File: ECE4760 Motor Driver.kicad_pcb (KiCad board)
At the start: 6 copper layers, 43.2 x 44.5 mm, 162 parts, among them J1 IO, J101 Alternative Motor, J2 Motor / Power, J3 UART, Q1 EPC23104, Q2 EPC23104, Q3 EPC23104, Q4 EPC23104, U1 STM32G473V_B-C-E_Hx, U2 ACS711xEXLT-15AB, U3 ACS711xEXLT-15AB, U4 ACS711xEXLT-15AB, U5 ACS711xEXLT-15AB, U6 AP7361C-33FGE, U7 TPSM365R6, X1 48MHz

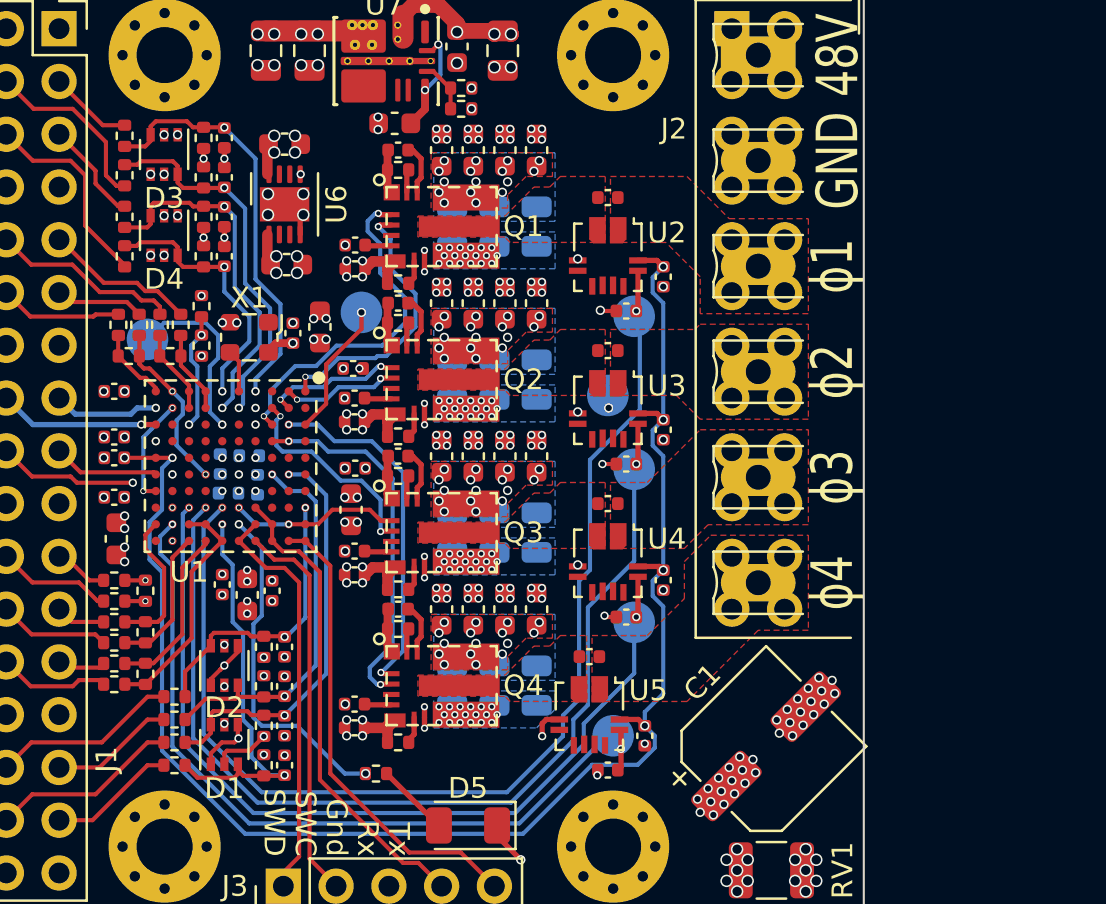
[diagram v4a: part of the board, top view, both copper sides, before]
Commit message: Change MCU package and MOSFETs
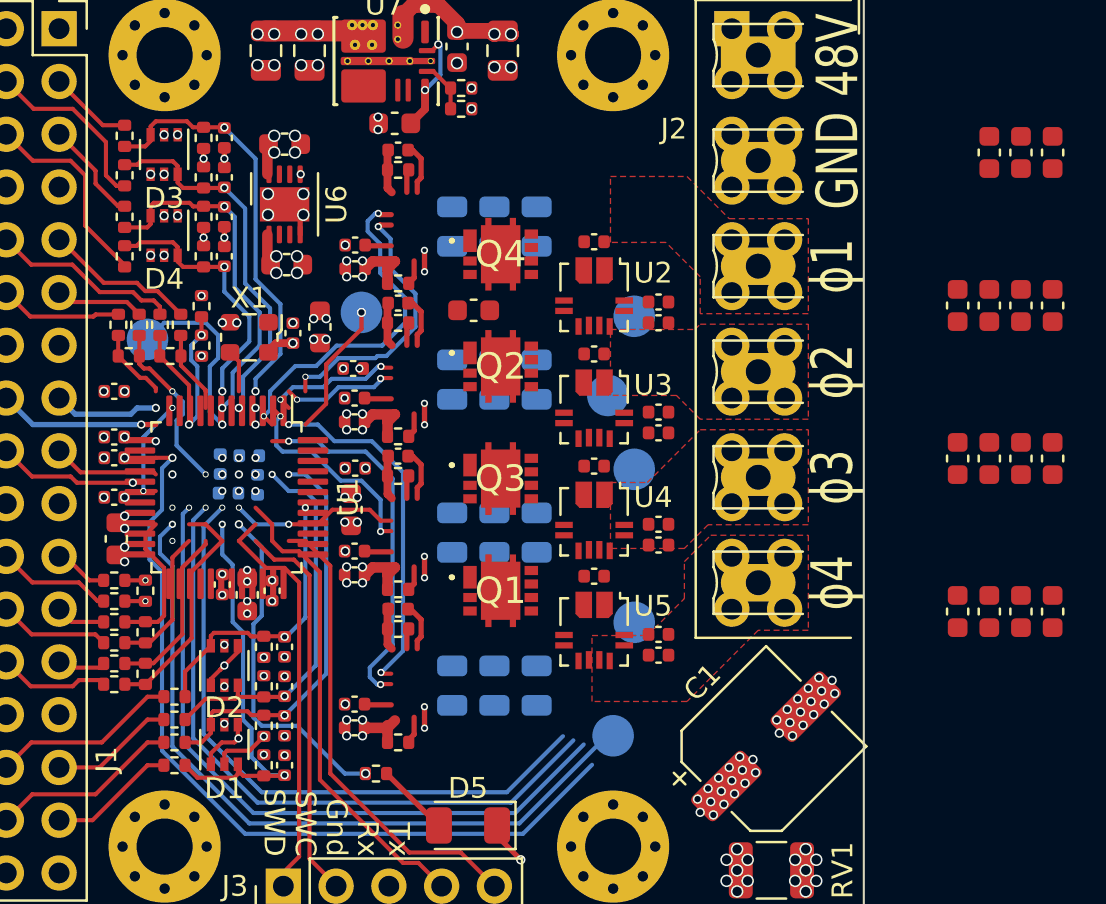
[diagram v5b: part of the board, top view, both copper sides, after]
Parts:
- Q1, Q2, Q3, Q4: value EPC23104 -> CSD87333Q3D; footprint EPC:EPC2310x -> CSD87333Q3D:CSD87333Q3D
- U1: value STM32G473V_B-C-E_Hx -> STM32G473CETx; footprint Package_BGA:TFBGA-100_8x8mm_Layout10x10_P0.8mm -> Package_QFP:LQFP-48_7x7mm_P0.5mm
- moved C12 24.8 mm to (128.5, 48.5)
- moved C22 24.8 mm to (123.9, 55.9)
- moved C23 24.8 mm to (125.4, 55.9)
- moved C25 24.8 mm to (128.5, 55.9)
- moved C35 24.8 mm to (123.9, 63.2)
- moved C36 24.8 mm to (125.4, 63.2)
- moved C38 24.8 mm to (128.5, 63.2)
- moved C48 24.8 mm to (123.9, 70.6)
- moved C49 24.8 mm to (125.4, 70.6)
- moved C51 24.8 mm to (128.5, 70.6)
- moved C9 24.8 mm to (125.4, 48.5)
- moved C11 24.8 mm to (126.9, 48.5)
- moved C24 24.8 mm to (126.9, 55.9)
- moved C37 24.8 mm to (126.9, 63.2)
- moved C50 24.8 mm to (126.9, 70.6)
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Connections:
- C17 pad 2: Net-(Q1-V_{DD}) -> unconnected-(C17-Pad2)
- C18 pad 1: Net-(Q1-V_{PHASE}) -> unconnected-(C18-Pad1)
- C18 pad 2: Net-(Q1-V_{BOOT}) -> Net-(C18-Pad2)
- C19 pad 1: Net-(Q1-SW) -> Net-(U2-IP-)
- C30 pad 2: Net-(Q2-V_{DD}) -> unconnected-(C30-Pad2)
- C31 pad 1: Net-(Q2-V_{PHASE}) -> unconnected-(C31-Pad1)
- C31 pad 2: Net-(Q2-V_{BOOT}) -> Net-(C31-Pad2)
- C32 pad 1: Net-(Q2-SW) -> Net-(U3-IP-)
- C43 pad 2: Net-(Q3-V_{DD}) -> unconnected-(C43-Pad2)
- C44 pad 1: Net-(Q3-V_{PHASE}) -> unconnected-(C44-Pad1)
- C44 pad 2: Net-(Q3-V_{BOOT}) -> Net-(C44-Pad2)
- C45 pad 1: Net-(Q3-SW) -> Net-(U4-IP-)
- C56 pad 2: Net-(Q4-V_{DD}) -> unconnected-(C56-Pad2)
- C57 pad 1: Net-(Q4-V_{PHASE}) -> unconnected-(C57-Pad1)
- C57 pad 2: Net-(Q4-V_{BOOT}) -> Net-(C57-Pad2)
- C58 pad 1: Net-(Q4-SW) -> Net-(U5-IP-)
- Q1 pad 1: /PH1_HI -> unconnected-(Q1-VIN-Pad1)
- Q1 pad 10: Vdrive -> unconnected-(Q1-PGND_2-Pad10)
- Q1 pad 11: Net-(Q1-V_{PHASE}) -> unconnected-(Q1-PGND_3-Pad11)
- Q1 pad 12: Net-(Q1-R_{BOOT}) -> unconnected-(Q1-PGND_4-Pad12)
- Q1 pad 13: Net-(Q1-V_{BOOT}) -> unconnected-(Q1-PGND_5-Pad13)
- Q1 pad 4: Net-(Q1-V_{DD}) -> unconnected-(Q1-TGR-Pad4)
- Q1 pad 5: +5V -> unconnected-(Q1-BG-Pad5)
- Q1 pad 6: Net-(Q1-R_{DRV}) -> unconnected-(Q1-VSW_1-Pad6)
- Q1 pad 7: GND -> unconnected-(Q1-VSW_2-Pad7)
- Q1 pad 8: GND -> unconnected-(Q1-VSW_3-Pad8)
- Q1 pad 9: Net-(Q1-SW) -> unconnected-(Q1-PGND_1-Pad9)
- Q2 pad 1: /PH2_HI -> unconnected-(Q2-VIN-Pad1)
- Q2 pad 10: Vdrive -> unconnected-(Q2-PGND_2-Pad10)
- Q2 pad 11: Net-(Q2-V_{PHASE}) -> unconnected-(Q2-PGND_3-Pad11)
- Q2 pad 12: Net-(Q2-R_{BOOT}) -> unconnected-(Q2-PGND_4-Pad12)
- Q2 pad 13: Net-(Q2-V_{BOOT}) -> unconnected-(Q2-PGND_5-Pad13)
- Q2 pad 4: Net-(Q2-V_{DD}) -> unconnected-(Q2-TGR-Pad4)
- Q2 pad 5: +5V -> unconnected-(Q2-BG-Pad5)
- Q2 pad 6: Net-(Q2-R_{DRV}) -> unconnected-(Q2-VSW_1-Pad6)
- Q2 pad 7: GND -> unconnected-(Q2-VSW_2-Pad7)
- Q2 pad 8: GND -> unconnected-(Q2-VSW_3-Pad8)
- Q2 pad 9: Net-(Q2-SW) -> unconnected-(Q2-PGND_1-Pad9)
- Q3 pad 1: /PH3_HI -> unconnected-(Q3-VIN-Pad1)
- Q3 pad 10: Vdrive -> unconnected-(Q3-PGND_2-Pad10)
- Q3 pad 11: Net-(Q3-V_{PHASE}) -> unconnected-(Q3-PGND_3-Pad11)
- Q3 pad 12: Net-(Q3-R_{BOOT}) -> unconnected-(Q3-PGND_4-Pad12)
- Q3 pad 13: Net-(Q3-V_{BOOT}) -> unconnected-(Q3-PGND_5-Pad13)
- Q3 pad 4: Net-(Q3-V_{DD}) -> unconnected-(Q3-TGR-Pad4)
- Q3 pad 5: +5V -> unconnected-(Q3-BG-Pad5)
- Q3 pad 6: Net-(Q3-R_{DRV}) -> unconnected-(Q3-VSW_1-Pad6)
- Q3 pad 7: GND -> unconnected-(Q3-VSW_2-Pad7)
- Q3 pad 8: GND -> unconnected-(Q3-VSW_3-Pad8)
- Q3 pad 9: Net-(Q3-SW) -> unconnected-(Q3-PGND_1-Pad9)
- Q4 pad 1: /PH4_HI -> unconnected-(Q4-VIN-Pad1)
- Q4 pad 10: Vdrive -> unconnected-(Q4-PGND_2-Pad10)
- Q4 pad 11: Net-(Q4-V_{PHASE}) -> unconnected-(Q4-PGND_3-Pad11)
- Q4 pad 12: Net-(Q4-R_{BOOT}) -> unconnected-(Q4-PGND_4-Pad12)
- Q4 pad 13: Net-(Q4-V_{BOOT}) -> unconnected-(Q4-PGND_5-Pad13)
- Q4 pad 4: Net-(Q4-V_{DD}) -> unconnected-(Q4-TGR-Pad4)
- Q4 pad 5: +5V -> unconnected-(Q4-BG-Pad5)
- Q4 pad 6: Net-(Q4-R_{DRV}) -> unconnected-(Q4-VSW_1-Pad6)
- Q4 pad 7: GND -> unconnected-(Q4-VSW_2-Pad7)
- Q4 pad 8: GND -> unconnected-(Q4-VSW_3-Pad8)
- Q4 pad 9: Net-(Q4-SW) -> unconnected-(Q4-PGND_1-Pad9)
- R10 pad 2: Net-(Q4-R_{DRV}) -> unconnected-(R10-Pad2)
- R11 pad 1: Net-(Q4-R_{BOOT}) -> unconnected-(R11-Pad1)
- R11 pad 2: Net-(Q4-V_{BOOT}) -> Net-(C57-Pad2)
- R30 pad 2: Net-(U1-PC9) -> unconnected-(R30-Pad2)
- R4 pad 2: Net-(Q1-R_{DRV}) -> unconnected-(R4-Pad2)
- R5 pad 1: Net-(Q1-R_{BOOT}) -> unconnected-(R5-Pad1)
- R5 pad 2: Net-(Q1-V_{BOOT}) -> Net-(C18-Pad2)
- R6 pad 2: Net-(Q2-R_{DRV}) -> unconnected-(R6-Pad2)
- R7 pad 1: Net-(Q2-R_{BOOT}) -> unconnected-(R7-Pad1)
- R7 pad 2: Net-(Q2-V_{BOOT}) -> Net-(C31-Pad2)
- R8 pad 2: Net-(Q3-R_{DRV}) -> unconnected-(R8-Pad2)
- R9 pad 1: Net-(Q3-R_{BOOT}) -> unconnected-(R9-Pad1)
- R9 pad 2: Net-(Q3-V_{BOOT}) -> Net-(C44-Pad2)
- U2 pad 2: Net-(Q1-SW) -> Net-(U2-IP-)
- U3 pad 2: Net-(Q2-SW) -> Net-(U3-IP-)
- U4 pad 2: Net-(Q3-SW) -> Net-(U4-IP-)
- U5 pad 2: Net-(Q4-SW) -> Net-(U5-IP-)
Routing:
- net (no net): track 0.00 -> 95.3 mm, vias 0 -> 16
- net +3V3: track 83.9 -> 50.2 mm, vias 30 -> 25
- net /PH1_SENSE: track 54.7 -> 30.9 mm, vias 2 -> 1
- net /PH4_LO: track 17.8 -> 0.00 mm, vias 2 -> 0
- net /PH4_HI: track 17.1 -> 0.00 mm, vias 2 -> 0
- net /PH1_HI: track 16.7 -> 0.00 mm, vias 2 -> 0
- net unconnected-(R30-Pad2): track 0.00 -> 16.4 mm, vias 0 -> 2
- net Net-(U1-PC9): track 16.4 -> 0.00 mm, vias 2 -> 0
- net /PH2_SENSE: track 48.4 -> 32.2 mm, vias 2 -> 1
- net /PH1_LO: track 13.2 -> 0.00 mm, vias 2 -> 0
- net /PH3_LO: track 10.2 -> 0.00 mm, vias 2 -> 0
- net /PH3_SENSE: track 42.4 -> 33.5 mm, vias 2 -> 1
- net /PH3_HI: track 8.17 -> 0.00 mm, vias 2 -> 0
- net /PH2_HI: track 6.59 -> 0.00 mm, vias 2 -> 0
- net /PH2_LO: track 5.59 -> 0.00 mm, vias 2 -> 0
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- removed copper zone on B.Cu, net GND
- removed copper zone on F.Cu, net Net-(Q1-SW)
- removed copper zone on F.Cu, net Net-(Q2-SW)
- removed copper zone on F.Cu, net Net-(Q3-SW)
- removed copper zone on F.Cu, net Net-(Q4-SW)
- removed copper zone on B.Cu, net Vdrive
- removed copper zone on F.Cu, net Vdrive

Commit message: Update
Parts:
- removed C14, C15, C26, C27, C28, C3, C39, C40, C41, C52, C53, C54: 1u, 100V, 0805, X7R, Capacitor_SMD:C_0805_2012Metric
- removed C17, C30, C43, C56, C68, C69, C74, C75, C76, C77, C78, C79, C80, C81, C82, C83, C84: 100n, Capacitor_SMD:C_0402_1005Metric
- removed C2, C23, C24, C25, C36, C37, C38, C49, C50, C51: 100n, 100V, 0603, X7R, Capacitor_SMD:C_0603_1608Metric
- removed C4, C5: 22u, Capacitor_SMD:C_0805_2012Metric
- removed C64: 1n, Capacitor_SMD:C_0402_1005Metric
- removed C7, C70, C71, C72, C73: 4u7, Capacitor_SMD:C_0603_1608Metric
- removed D1, D2, D3, D4: BAT54XY, Package_TO_SOT_SMD:SOT-363_SC-70-6
- removed R1: 40k2, Resistor_SMD:R_0402_1005Metric
- removed R18, R26: 4k7, Resistor_SMD:R_0402_1005Metric
- removed R19, R27: 100, Resistor_SMD:R_0402_1005Metric
- removed R28, R29: 1k, Resistor_SMD:R_0402_1005Metric
- removed R3: 10k, Resistor_SMD:R_0402_1005Metric
- removed R40, R41, R42, R43, R44, R45: 1k, 1%, Resistor_SMD:R_0402_1005Metric
- removed TP1: RESET, TestPoint:TestPoint_Pad_D2.0mm
- removed TP2: BOOT, TestPoint:TestPoint_Pad_D2.0mm
- removed U7: TPSM365R6, TPSM:RDN0011A-MFG
- added D6: Green, LED_SMD:LED_1206_3216Metric, F.Cu at (112.1, 43.3)
- added L1: 4u7, Inductor_SMD:L_1008_2520Metric, F.Cu at (89.4, 70.8)
- added R2: 330, Resistor_SMD:R_0402_1005Metric, F.Cu at (95.4, 81.4)
- added SW1: RESET, Button_Switch_SMD:SW_SPST_PTS810, F.Cu at (100.8, 43.2)
- added U10: DGD05473FNQ, Package_DFN_QFN:DFN-10-1EP_3x3mm_P0.5mm_EP1.65x2.38mm, F.Cu at (94.1, 55.0)
- added U11: DGD05473FNQ, Package_DFN_QFN:DFN-10-1EP_3x3mm_P0.5mm_EP1.65x2.38mm, F.Cu at (94.1, 60.4)
- added U12: DGD05473FNQ, Package_DFN_QFN:DFN-10-1EP_3x3mm_P0.5mm_EP1.65x2.38mm, F.Cu at (94.1, 65.8)
- added U13: AP63205WU, Package_TO_SOT_SMD:TSOT-23-6, F.Cu at (89.4, 74.8)
- added U8: DGD05473FNQ, Package_DFN_QFN:DFN-10-1EP_3x3mm_P0.5mm_EP1.65x2.38mm, F.Cu at (94.1, 49.6)
- added U9: MAX13433EETD, Package_DFN_QFN:DFN-14-1EP_3x3mm_P0.4mm_EP1.78x2.35mm, F.Cu at (82.8, 69.2)
- C1: footprint Capacitor_SMD:CP_Elec_6.3x7.7 -> Capacitor_THT:CP_Radial_D6.3mm_P2.50mm
- C10, C11: value 100n, 100V, 0603, X7R -> 22u; footprint Capacitor_SMD:C_0603_1608Metric -> Capacitor_SMD:C_0805_2012Metric
- C12: value 100n, 100V, 0603, X7R -> 10u; footprint Capacitor_SMD:C_0603_1608Metric -> Capacitor_SMD:C_0805_2012Metric
- C13: value 1u, 100V, 0805, X7R -> 100n; footprint Capacitor_SMD:C_0805_2012Metric -> Capacitor_SMD:C_0402_1005Metric; moved to F.Cu
- C16, C29, C42, C55: value 1u -> 100n
- J1: footprint Connector_PinSocket_2.54mm:PinSocket_2x17_P2.54mm_Vertical -> Connector_PinSocket_2.54mm:PinSocket_2x14_P2.54mm_Vertical
- J3: footprint Connector_PinHeader_2.54mm:PinHeader_1x05_P2.54mm_Vertical -> Connector_PinHeader_2.54mm:PinHeader_2x04_P2.54mm_Vertical
- RV1: value 60V 250A -> 26V 200A
- moved C11 45.7 mm to (87.0, 70.6), turned to -90 degrees
- moved C12 44.9 mm to (92.1, 74.8)
- moved D5 41.4 mm to (117.6, 43.3), turned to -90 degrees
- moved J3 38.9 mm to (87.9, 45.1)
- moved R15 30.4 mm to (80.8, 48.1), turned to -90 degrees
- moved J101 29.7 mm to (141.2, 51.9)
- moved R14 29.6 mm to (80.8, 50.0), turned to 90 degrees
- moved R13 29.1 mm to (81.8, 48.1), turned to -90 degrees
- moved C62 28.2 mm to (80.8, 51.9), turned to -90 degrees
- moved R12 27.5 mm to (81.8, 50.0)
- moved R17 26.8 mm to (82.8, 48.1), turned to -90 degrees
- moved C61 26.1 mm to (81.8, 51.9)
- moved C9 24.7 mm to (100.8, 46.7), turned to 0 degrees
- moved C13 24.6 mm to (87.2, 73.3), turned to 90 degrees
- moved C48 24.3 mm to (100.8, 62.9), turned to 0 degrees
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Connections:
- net LED_1 renamed CLK+
- net LED_2 renamed CLK-
- net ~{Abort} renamed DATA-
- C10 pad 1: Vdrive -> +5V
- C11 pad 1: Vdrive -> +5V
- C13 pad 1: Vdrive -> Net-(U13-BST)
- C13 pad 2: GND -> Net-(U13-SW)
- C18 pad 1: unconnected-(C18-Pad1) -> Net-(U8-VB)
- C18 pad 2: Net-(C18-Pad2) -> Net-(Q1-TGR)
- C31 pad 1: unconnected-(C31-Pad1) -> Net-(U10-VB)
- C31 pad 2: Net-(C31-Pad2) -> Net-(Q2-TGR)
- C44 pad 1: unconnected-(C44-Pad1) -> Net-(U11-VB)
- C44 pad 2: Net-(C44-Pad2) -> Net-(Q3-TGR)
- C57 pad 1: unconnected-(C57-Pad1) -> Net-(U12-VB)
- C57 pad 2: Net-(C57-Pad2) -> Net-(Q4-TGR)
- C61 pad 1: /HALL_C -> /HALL_B
- C62 pad 1: /HALL_I -> /HALL_C
- C63 pad 1: /HALL_B -> /HALL_A
- J1 pad 1: +5V -> unconnected-(J1-Pin_1-Pad1)
- J1 pad 10: Aux_Enc_B_In- -> Hall_B_In
- J1 pad 11: Aux_Enc_A_In- -> Hall_I_In
- J1 pad 12: Aux_Enc_A_In+ -> Hall_C_In
- J1 pad 13: +5V -> unconnected-(J1-Pin_13-Pad13)
- J1 pad 14: GND -> unconnected-(J1-Pin_14-Pad14)
- J1 pad 17: ~{Fault_Enable} -> DATA+
- J1 pad 19: +3V3 -> unconnected-(J1-Pin_19-Pad19)
- J1 pad 2: GND -> unconnected-(J1-Pin_2-Pad2)
- J1 pad 20: GND -> unconnected-(J1-Pin_20-Pad20)
- J1 pad 27: +5V -> unconnected-(J1-Pin_27-Pad27)
- J1 pad 28: GND -> unconnected-(J1-Pin_28-Pad28)
- J1 pad 7: +5V -> unconnected-(J1-Pin_7-Pad7)
- J1 pad 8: GND -> unconnected-(J1-Pin_8-Pad8)
- J1 pad 9: Aux_Enc_B_In+ -> Hall_A_In
- J2 pad 1: Vdrive -> PH1
- J2 pad 2: GND -> PH2
- J2 pad 3: PH1 -> PH3
- J2 pad 4: PH2 -> PH4
- J2 pad 5: PH3 -> Vdrive
- J2 pad 6: PH4 -> GND
- J3 pad 2: /UART_TX -> /SWCLK
- J3 pad 3: GND -> /UART_TX
- J3 pad 5: /SWCLK -> GND
- Q1 pad 1: unconnected-(Q1-VIN-Pad1) -> Vdrive
- Q1 pad 10: unconnected-(Q1-PGND_2-Pad10) -> GND
- Q1 pad 11: unconnected-(Q1-PGND_3-Pad11) -> GND
- Q1 pad 12: unconnected-(Q1-PGND_4-Pad12) -> GND
- Q1 pad 13: unconnected-(Q1-PGND_5-Pad13) -> GND
- Q1 pad 3: unconnected-(Q1-TG-Pad3) -> Net-(Q1-TG)
- Q1 pad 4: unconnected-(Q1-TGR-Pad4) -> Net-(Q1-TGR)
- Q1 pad 5: unconnected-(Q1-BG-Pad5) -> Net-(Q1-BG)
- Q1 pad 6: unconnected-(Q1-VSW_1-Pad6) -> Net-(U2-IP-)
- Q1 pad 7: unconnected-(Q1-VSW_2-Pad7) -> Net-(U2-IP-)
- Q1 pad 8: unconnected-(Q1-VSW_3-Pad8) -> Net-(U2-IP-)
- Q1 pad 9: unconnected-(Q1-PGND_1-Pad9) -> GND
- Q2 pad 1: unconnected-(Q2-VIN-Pad1) -> Vdrive
- Q2 pad 10: unconnected-(Q2-PGND_2-Pad10) -> GND
- Q2 pad 11: unconnected-(Q2-PGND_3-Pad11) -> GND
- Q2 pad 12: unconnected-(Q2-PGND_4-Pad12) -> GND
- Q2 pad 13: unconnected-(Q2-PGND_5-Pad13) -> GND
- Q2 pad 3: unconnected-(Q2-TG-Pad3) -> Net-(Q2-TG)
- Q2 pad 4: unconnected-(Q2-TGR-Pad4) -> Net-(Q2-TGR)
- Q2 pad 5: unconnected-(Q2-BG-Pad5) -> Net-(Q2-BG)
- Q2 pad 6: unconnected-(Q2-VSW_1-Pad6) -> Net-(U3-IP-)
- Q2 pad 7: unconnected-(Q2-VSW_2-Pad7) -> Net-(U3-IP-)
- Q2 pad 8: unconnected-(Q2-VSW_3-Pad8) -> Net-(U3-IP-)
- Q2 pad 9: unconnected-(Q2-PGND_1-Pad9) -> GND
- Q3 pad 1: unconnected-(Q3-VIN-Pad1) -> Vdrive
- Q3 pad 10: unconnected-(Q3-PGND_2-Pad10) -> GND
- Q3 pad 11: unconnected-(Q3-PGND_3-Pad11) -> GND
- Q3 pad 12: unconnected-(Q3-PGND_4-Pad12) -> GND
- Q3 pad 13: unconnected-(Q3-PGND_5-Pad13) -> GND
- Q3 pad 3: unconnected-(Q3-TG-Pad3) -> Net-(Q3-TG)
- Q3 pad 4: unconnected-(Q3-TGR-Pad4) -> Net-(Q3-TGR)
- Q3 pad 5: unconnected-(Q3-BG-Pad5) -> Net-(Q3-BG)
- Q3 pad 6: unconnected-(Q3-VSW_1-Pad6) -> Net-(U4-IP-)
- Q3 pad 7: unconnected-(Q3-VSW_2-Pad7) -> Net-(U4-IP-)
- Q3 pad 8: unconnected-(Q3-VSW_3-Pad8) -> Net-(U4-IP-)
- Q3 pad 9: unconnected-(Q3-PGND_1-Pad9) -> GND
- Q4 pad 1: unconnected-(Q4-VIN-Pad1) -> Vdrive
- Q4 pad 10: unconnected-(Q4-PGND_2-Pad10) -> GND
- Q4 pad 11: unconnected-(Q4-PGND_3-Pad11) -> GND
- Q4 pad 12: unconnected-(Q4-PGND_4-Pad12) -> GND
- Q4 pad 13: unconnected-(Q4-PGND_5-Pad13) -> GND
- Q4 pad 3: unconnected-(Q4-TG-Pad3) -> Net-(Q4-TG)
- Q4 pad 4: unconnected-(Q4-TGR-Pad4) -> Net-(Q4-TGR)
- Q4 pad 5: unconnected-(Q4-BG-Pad5) -> Net-(Q4-BG)
- Q4 pad 6: unconnected-(Q4-VSW_1-Pad6) -> Net-(U5-IP-)
- Q4 pad 7: unconnected-(Q4-VSW_2-Pad7) -> Net-(U5-IP-)
- Q4 pad 8: unconnected-(Q4-VSW_3-Pad8) -> Net-(U5-IP-)
- Q4 pad 9: unconnected-(Q4-PGND_1-Pad9) -> GND
- R10 pad 1: +5V -> Net-(Q4-TG)
- R10 pad 2: unconnected-(R10-Pad2) -> Net-(U12-HO)
- R11 pad 1: unconnected-(R11-Pad1) -> Net-(U12-LO)
- R11 pad 2: Net-(C57-Pad2) -> Net-(Q4-BG)
- R12 pad 2: /HALL_C -> /HALL_B
- R13 pad 1: Hall_C_In -> Hall_B_In
- R13 pad 2: /HALL_C -> /HALL_B
- R14 pad 2: /HALL_I -> /HALL_C
- R15 pad 1: Hall_I_In -> Hall_C_In
- R15 pad 2: /HALL_I -> /HALL_C
- R16 pad 2: /HALL_B -> /HALL_A
- R17 pad 1: Hall_B_In -> Hall_A_In
- R17 pad 2: /HALL_B -> /HALL_A
- R30 pad 1: Net-(D5-A) -> Net-(U1-PA6)
- R30 pad 2: unconnected-(R30-Pad2) -> Net-(D5-A)
- R31 pad 1: Enc_A_In+ -> Enc_I_In+
- R31 pad 2: /ENC_A+ -> /ENC_I+
- R32 pad 1: /ENC_A- -> /ENC_I-
- R32 pad 2: /ENC_A+ -> /ENC_I+
- R33 pad 1: Enc_A_In- -> Enc_I_In-
- R33 pad 2: /ENC_A- -> /ENC_I-
- R34 pad 1: Enc_B_In+ -> Enc_A_In+
- R34 pad 2: /ENC_B+ -> /ENC_A+
- R35 pad 1: /ENC_B- -> /ENC_A-
- R35 pad 2: /ENC_B+ -> /ENC_A+
- R36 pad 1: Enc_B_In- -> Enc_A_In-
- R36 pad 2: /ENC_B- -> /ENC_A-
- R37 pad 1: Enc_I_In+ -> Enc_B_In+
- R37 pad 2: /ENC_I+ -> /ENC_B+
- R38 pad 1: /ENC_I- -> /ENC_B-
- R38 pad 2: /ENC_I+ -> /ENC_B+
- R39 pad 1: Enc_I_In- -> Enc_B_In-
- R39 pad 2: /ENC_I- -> /ENC_B-
- R4 pad 1: +5V -> Net-(Q1-TG)
- R4 pad 2: unconnected-(R4-Pad2) -> Net-(U8-HO)
- R5 pad 1: unconnected-(R5-Pad1) -> Net-(U8-LO)
- R5 pad 2: Net-(C18-Pad2) -> Net-(Q1-BG)
- R6 pad 1: +5V -> Net-(Q2-TG)
- R6 pad 2: unconnected-(R6-Pad2) -> Net-(U10-HO)
- R7 pad 1: unconnected-(R7-Pad1) -> Net-(U10-LO)
- R7 pad 2: Net-(C31-Pad2) -> Net-(Q2-BG)
- R8 pad 1: +5V -> Net-(Q3-TG)
- R8 pad 2: unconnected-(R8-Pad2) -> Net-(U11-HO)
- R9 pad 1: unconnected-(R9-Pad1) -> Net-(U11-LO)
- R9 pad 2: Net-(C44-Pad2) -> Net-(Q3-BG)
- U1 pad 1: unconnected-(U1-VBAT-Pad1) -> +3V3
- U1 pad 10: unconnected-(U1-PA2-Pad10) -> /HALL_C
- U1 pad 11: unconnected-(U1-PA3-Pad11) -> Net-(U1-PA3)
- U1 pad 12: unconnected-(U1-PA4-Pad12) -> /ENC_I-
- U1 pad 13: unconnected-(U1-PA5-Pad13) -> /ENC_A-
- U1 pad 14: unconnected-(U1-PA6-Pad14) -> Net-(U1-PA6)
- U1 pad 15: unconnected-(U1-PA7-Pad15) -> /ENC_A+
- U1 pad 16: unconnected-(U1-PB0-Pad16) -> /ENC_B+
- U1 pad 17: unconnected-(U1-PB1-Pad17) -> /ENC_I+
- U1 pad 18: unconnected-(U1-PB2-Pad18) -> /ENC_B-
- U1 pad 19: unconnected-(U1-VSSA-Pad19) -> GND
- U1 pad 2: unconnected-(U1-PC13-Pad2) -> /LIM_L
- U1 pad 21: unconnected-(U1-VDDA-Pad21) -> +3V3
- U1 pad 23: Net-(U1-VSS-Pad23) -> GND
- U1 pad 24: unconnected-(U1-VDD-Pad24) -> +3V3
- U1 pad 25: unconnected-(U1-PB11-Pad25) -> /PH4_SENSE
- U1 pad 26: unconnected-(U1-PB12-Pad26) -> /PH3_SENSE
- U1 pad 27: unconnected-(U1-PB13-Pad27) -> /PH2_SENSE
- U1 pad 28: unconnected-(U1-PB14-Pad28) -> /PH1_SENSE
- U1 pad 29: unconnected-(U1-PB15-Pad29) -> /PH2_LO
- U1 pad 3: unconnected-(U1-PC14-Pad3) -> /LIM_R
- U1 pad 30: unconnected-(U1-PA8-Pad30) -> /PH4_HI
- U1 pad 31: unconnected-(U1-PA9-Pad31) -> /PH3_HI
- U1 pad 32: unconnected-(U1-PA10-Pad32) -> /PH2_HI
- U1 pad 33: unconnected-(U1-PA11-Pad33) -> /PH4_LO
- U1 pad 34: unconnected-(U1-PA12-Pad34) -> /PH3_LO
- U1 pad 35: Net-(U1-VSS-Pad23) -> GND
- U1 pad 36: unconnected-(U1-VDD-Pad36) -> +3V3
- U1 pad 37: unconnected-(U1-PA13-Pad37) -> /SWDIO
- U1 pad 38: unconnected-(U1-PA14-Pad38) -> /SWCLK
- U1 pad 39: unconnected-(U1-PA15-Pad39) -> ~{Fault_Enable}
- U1 pad 4: unconnected-(U1-PC15-Pad4) -> /LIM_H
- U1 pad 40: unconnected-(U1-PB3-Pad40) -> Net-(U1-PB3)
- U1 pad 41: unconnected-(U1-PB4-Pad41) -> Net-(U1-PB4)
- U1 pad 42: unconnected-(U1-PB5-Pad42) -> /PH1_LO
- U1 pad 43: unconnected-(U1-PB6-Pad43) -> /UART_TX
- U1 pad 44: unconnected-(U1-PB7-Pad44) -> /UART_RX
- U1 pad 45: unconnected-(U1-PB8-Pad45) -> /BOOT
- U1 pad 46: unconnected-(U1-PB9-Pad46) -> /PH1_HI
- U1 pad 47: Net-(U1-VSS-Pad23) -> GND
- U1 pad 48: unconnected-(U1-VDD-Pad48) -> +3V3
- U1 pad 5: unconnected-(U1-PF0-Pad5) -> /OSC_IN
- U1 pad 7: unconnected-(U1-PG10-Pad7) -> /~{RST}
- U1 pad 8: unconnected-(U1-PA0-Pad8) -> /HALL_A
- U1 pad 9: unconnected-(U1-PA1-Pad9) -> /HALL_B
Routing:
- net (no net): track 95.3 -> 0.00 mm, vias 16 -> 0
- net /PH4_SENSE: track 34.9 -> 0.00 mm, vias 1 -> 0
- net /PH3_SENSE: track 33.5 -> 0.00 mm, vias 1 -> 0
- net /PH2_SENSE: track 32.2 -> 0.00 mm, vias 1 -> 0
- net /PH1_SENSE: track 30.9 -> 0.00 mm, vias 1 -> 0
- net +3V3: track 50.2 -> 21.7 mm, vias 25 -> 0
- net /SWDIO: track 22.8 -> 0.00 mm, vias 0 -> 1
- net +5V: track 24.0 -> 2.29 mm, vias 29 -> 3
- net /SWCLK: track 22.6 -> 0.92 mm, vias 0 -> 1
- net /LIM_R: track 20.2 -> 0.00 mm, vias 2 -> 0
- net /HALL_I: track 19.9 -> 0.00 mm, vias 2 -> 0
- net /HALL_C: track 19.7 -> 0.00 mm, vias 2 -> 0
- net /UART_RX: track 18.9 -> 0.00 mm
- net /UART_TX: track 18.8 -> 0.00 mm
- net /HALL_A: track 18.5 -> 0.00 mm, vias 2 -> 0
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- added copper zone on B.Cu, net GND
- added copper zone on In2.Cu, net GND
- added copper zone on F.Cu, net Net-(U2-IP-)
- added copper zone on F.Cu, net Net-(U3-IP-)
- added copper zone on F.Cu, net Net-(U4-IP-)
- added copper zone on F.Cu, net Net-(U5-IP-)
- added copper zone on F.Cu, net Vdrive
- removed copper zone on In2.Cu, net +3V3
- removed copper zone on In2.Cu, net +5V
- removed copper zone on In3.Cu, net GND
- removed copper zone on In4.Cu, net GND
- removed copper zone on In2.Cu, net Vdrive
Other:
- board size 43.2 x 44.5 mm -> 45.7 x 36.8 mm
- copper layers 6 -> 4
